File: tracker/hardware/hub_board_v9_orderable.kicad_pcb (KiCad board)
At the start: 4 copper layers, 103 x 103 mm, 39 parts, among them U1 ESP32-S3-WROOM-1U-N8R8, U2 LoRa2021F33-2G4, U3 LoRa2021_Castellated, U4 SX1280, U5 MAX-M10S, U6 MS5611-01BA, U7 TPS7A02

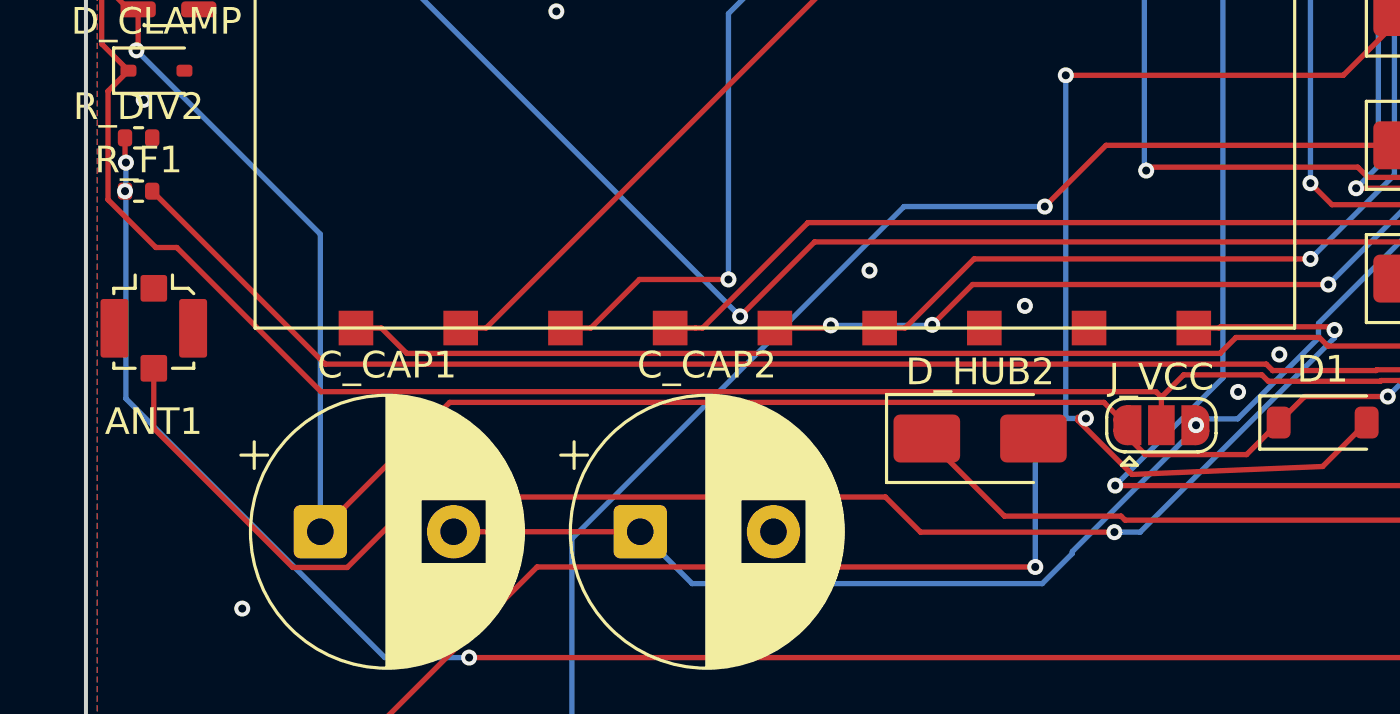
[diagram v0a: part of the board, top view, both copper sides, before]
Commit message: fix(pcb): eliminate the last 2 REAL shorts -- 3 local B.Cu detours
MEASURED 2026-10-12, chain: clear_hub_v9_wedged_plane_pads.py ->
throughify_inplace.py -> refill_hub_v9_zones.py on hub_board_v9_final.

  agentee short        2 -> 0   *** clean ***
  agentee via-lamination  GONE  (JLCPCB blind-via blocker stays solved)
  blind vias           18 -> 0
  KiCad violations     84 -> 83

The 3 offending B.Cu segments were detoured locally (< 0.8 mm apex):
  /SCAP_ADC  d=0.035 -> apex (2.165,17.515)
  /SCAP_MID  d=0.414 -> apex (42.217,25.892)
  /SCAP_MID  d=0.071 -> apex (42.140,26.790)
The vias did NOT move (they are via-in-pad at offset +0,+0 um and moving breaks
the pad connection -- proven by the relocate+stub attempt which made 5 shorts).

RESIDUAL (new, from the detour, measured): 4 clearance grazes 0.014-0.14 mm vs
the 0.15 mm rule, and 2 dangling-track apexes. The detour needs a
clearance-aware router pass (or a bigger, net-aware apex push) -- six blind-nudge
attempts have now each produced a new sub-rule graze somewhere, so this is the
last hand-nudge: from here the fix is FreeRouting/agentee route, not scripting.

NOT shippable yet: 4 clearance grazes are real.
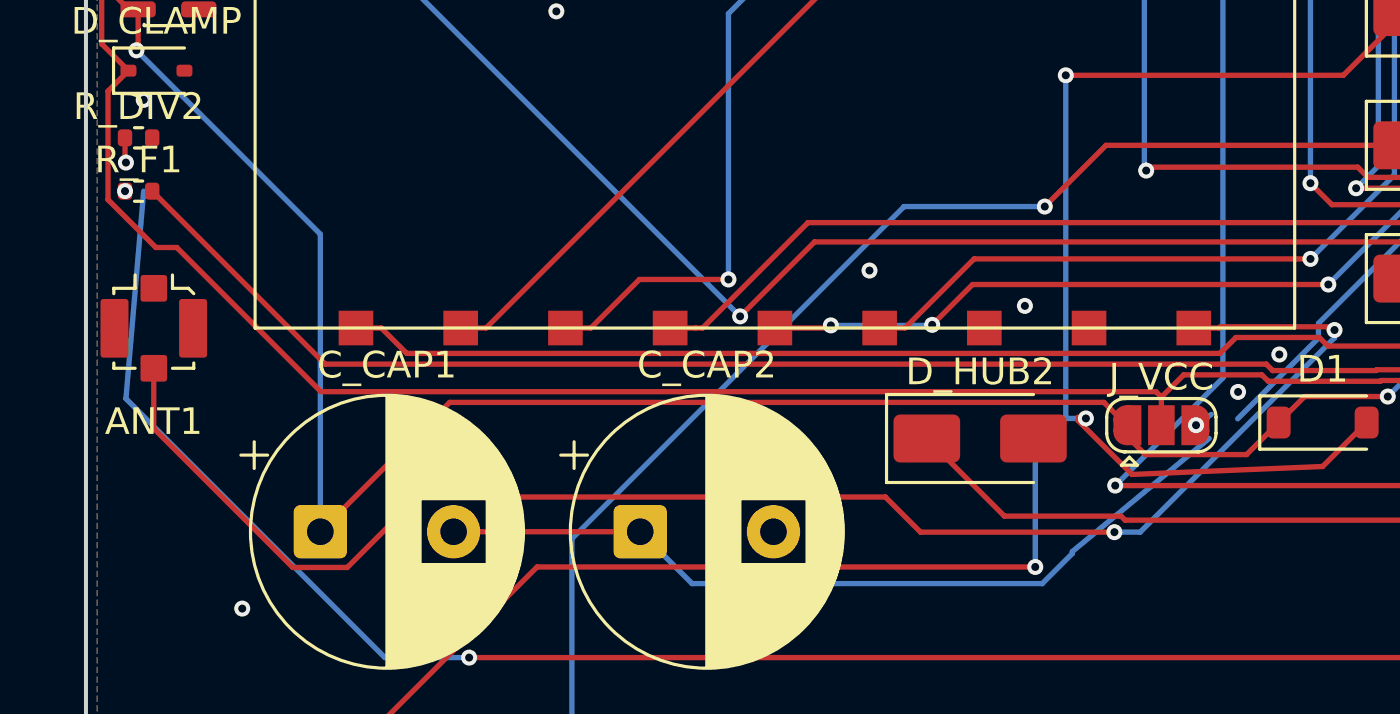
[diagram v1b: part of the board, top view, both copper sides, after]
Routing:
- net /SCAP_MID: track 61.8 -> 60.5 mm
- net /SCAP_ADC: track 94.5 -> 93.5 mm
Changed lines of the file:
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@@
+	)
+	(segment
+		(start 2.165 17.515)
+		(end 2.165 17.515)
+		(width 0.2)
+		(layer "B.Cu")
+		(net 29)
 	)
 	(segment
 		(start 1.4998 25.2991)
-		(end 1.4998 16.4437)
+		(end 2.165 17.515)
 		(width 0.2)
 		(layer "B.Cu")
@@
 	(segment
 		(start 41.9836 26.0563)
-		(end 43.2077 26.0563)
+		(end 42.217125 25.891673)
 		(width 0.2)
 		(layer "B.Cu")
@@
 	)
 	(segment
+		(start 42.139974 26.789974)
+		(end 42.139974 26.789974)
+		(width 0.2)
+		(layer "B.Cu")
+		(net 30)
+	)
+	(segment
 		(start 37.0049 31.035)
-		(end 41.9836 26.0563)
+		(end 42.139974 26.789974)
 		(width 0.2)
 		(layer "B.Cu")
@@
 		(width 0.2)
 		(layer "B.Cu")
+		(net 30)
+	)
+	(segment
+		(start 42.217125 25.891673)
+		(end 42.217125 25.891673)
+		(width 0.2)
+		(layer "B.Cu")

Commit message: feat(pcb): add 3 fiducials + tooling holes -- both JLCPCB reqs now SATISFIED
MEASURED 2026-10-12. add_hub_v9_fab_marks.py on the orderable board:

  agentee fiducials      1 -> 0   *** satisfied ***
  agentee tooling-holes  1 -> 0   *** satisfied ***
  agentee short          1 -> 0
  3 fiducials + 2 tooling holes placed; 0 shorts, KiCad-clean additions

KEY FIX: agentee's rule text is "no footprint named like 'Fiducial' on the
board" -- it matches the footprint LIBRARY NAME (LIB_ID), not the reference.
Setting only SetReference("FID1") left the rule firing even with 3 pads
placed. Fix = SetFPID(LIB_ID("Fiducial", ...)) / LIB_ID("MountingHole", ...).

Two placement-search bugs found and fixed by measurement:
  1. cell_clear tested pad CENTRE, so a fiducial landed inside a 4.0x1.2 mm
     J_W3 pad (reaches x=98.0) and shorted J_W3.2 -> now tests pad EXTENT.
  2. the Edge.Cuts board outline on this board is ONE degenerate (0,0)-(103,103)
     diagonal segment, so any bbox test against Edge.Cuts rejects every cell ->
     removed that test; pad extents already cover the sockets.

Fiducial positions (3, widely separated, non-collinear for a usable datum):
  FID1 (5.425,5.425)  FID2 (5.425,97.575)  FID3 (96.425,52.425)
Tooling holes: TH1 (9.425,9.425)  TH2 (9.425,93.575)  [3rd blocked by J_W3]

NEXT: agentee 'tie' is the correct fix for via-in-pad -- 'Tie every SMD pad of
a plane net to its plane with a stub and a via BESIDE the pad'. That replaces
the via-in-pad approach (vias must not sit in pads).
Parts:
- added FID1: Fiducial, Fiducial:Fiducial_1mm_Mask2mm, F.Cu at (5.42, 5.42)
- added FID3: Fiducial, Fiducial:Fiducial_1mm_Mask2mm, F.Cu at (96.4, 52.4)
- added FID3: Fiducial, Fiducial:Fiducial_1mm_Mask2mm, F.Cu at (5.42, 97.6)
- added TH1: MountingHole, MountingHole:MountingHole_1.5mm, F.Cu at (9.43, 9.43)
- added TH2: MountingHole, MountingHole:MountingHole_1.5mm, F.Cu at (9.43, 93.6)
